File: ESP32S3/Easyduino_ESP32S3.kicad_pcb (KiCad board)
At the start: 4 copper layers, 25.9 x 63.9 mm, 33 parts, among them J1 USB_C_Receptacle_USB2.0, J2 USB_C_Receptacle_USB2.0, Q1 Q_NPN_BCE, Q2 Q_NPN_BCE, SW1 SW_Push, SW2 SW_Push, U1 ESP32-S3-WROOM-1, U2 ESP32-S3-DevKitC, U3 CP2102N-Axx-xQFN28, U5 AMS1117-3.3

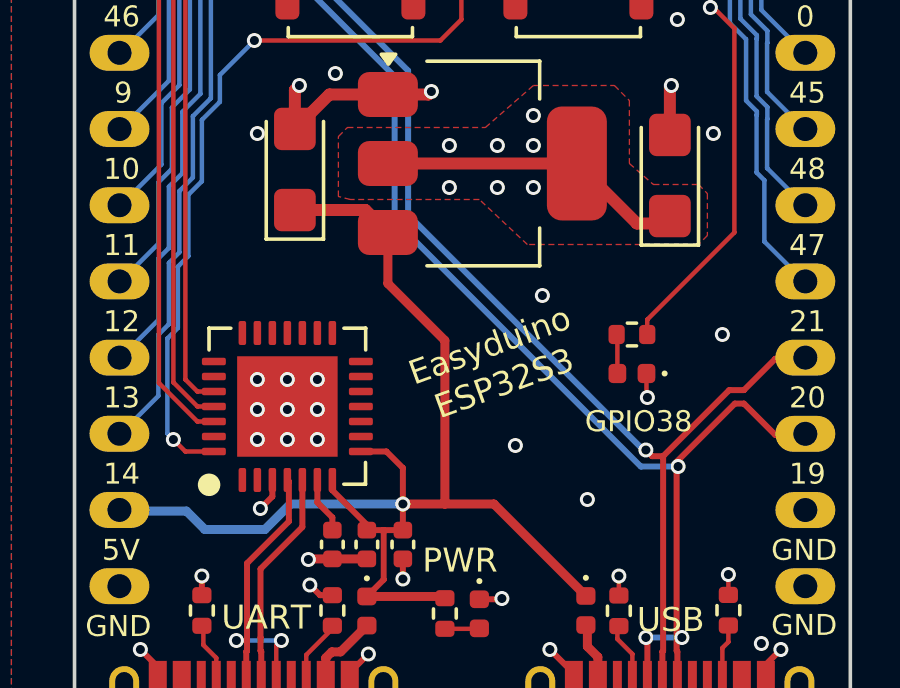
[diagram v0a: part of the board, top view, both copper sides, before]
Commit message: ESP32S3 CP2102 bugfix
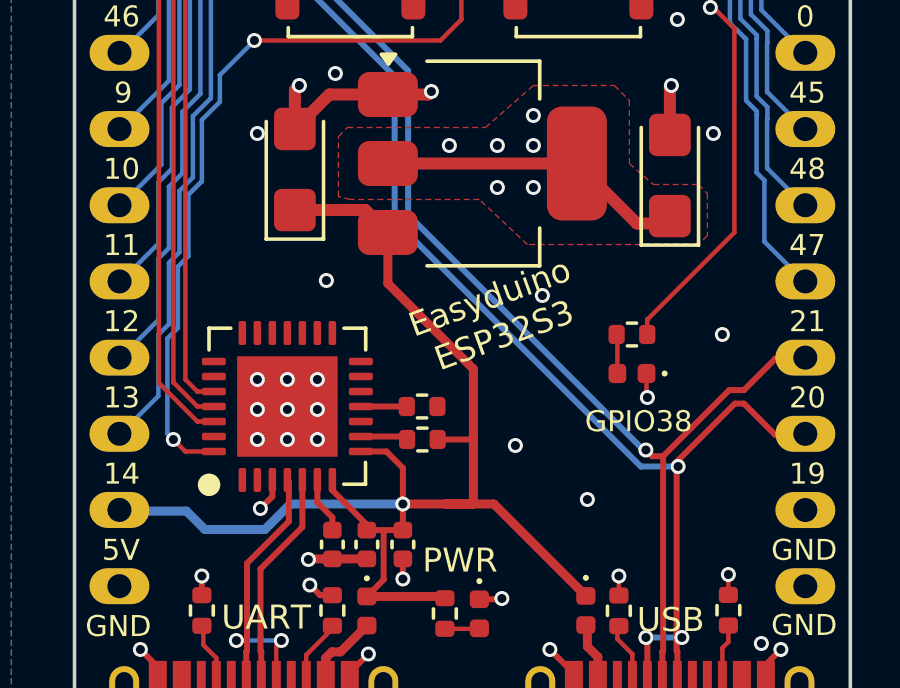
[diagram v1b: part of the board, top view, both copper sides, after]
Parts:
- added R10: 10k, Resistor_SMD:R_0402_1005Metric, F.Cu at (138.7, 107.1)
- added R11: 5.1k, Resistor_SMD:R_0402_1005Metric, F.Cu at (138.7, 108.2)
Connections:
- net +5V renamed VBUS
- U3 pad 11: unconnected-(U3-~{SUSPEND}-Pad11) -> /~{SUSPEND}
- U3 pad 9: unconnected-(U3-~{RST}-Pad9) -> /~{RST}
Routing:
- net VBUS: track 42.8 -> 45.3 mm
- net /~{RST}: track 0.00 -> 1.58 mm
- net /~{SUSPEND}: track 0.00 -> 1.53 mm
- net GND: vias 77 -> 78
- net +3.3V: vias 10 -> 9

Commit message: ESP32S3 v1.2
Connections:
- U3 pad 25: /GPIO44 -> /GPIO43
- U3 pad 26: /GPIO43 -> /GPIO44
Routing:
- net /GPIO43: track 58.2 -> 57.1 mm
